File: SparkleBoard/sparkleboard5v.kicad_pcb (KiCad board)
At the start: 2 copper layers, 33.4 x 29.7 mm, 33 parts, among them J3 Conn_01x04_Pin, J4 Conn_01x02_Pin, J5 Conn_01x02_Pin, U1 C9900066641, U2 AONR21307, U3 HUSB238, U6 AP63205WU

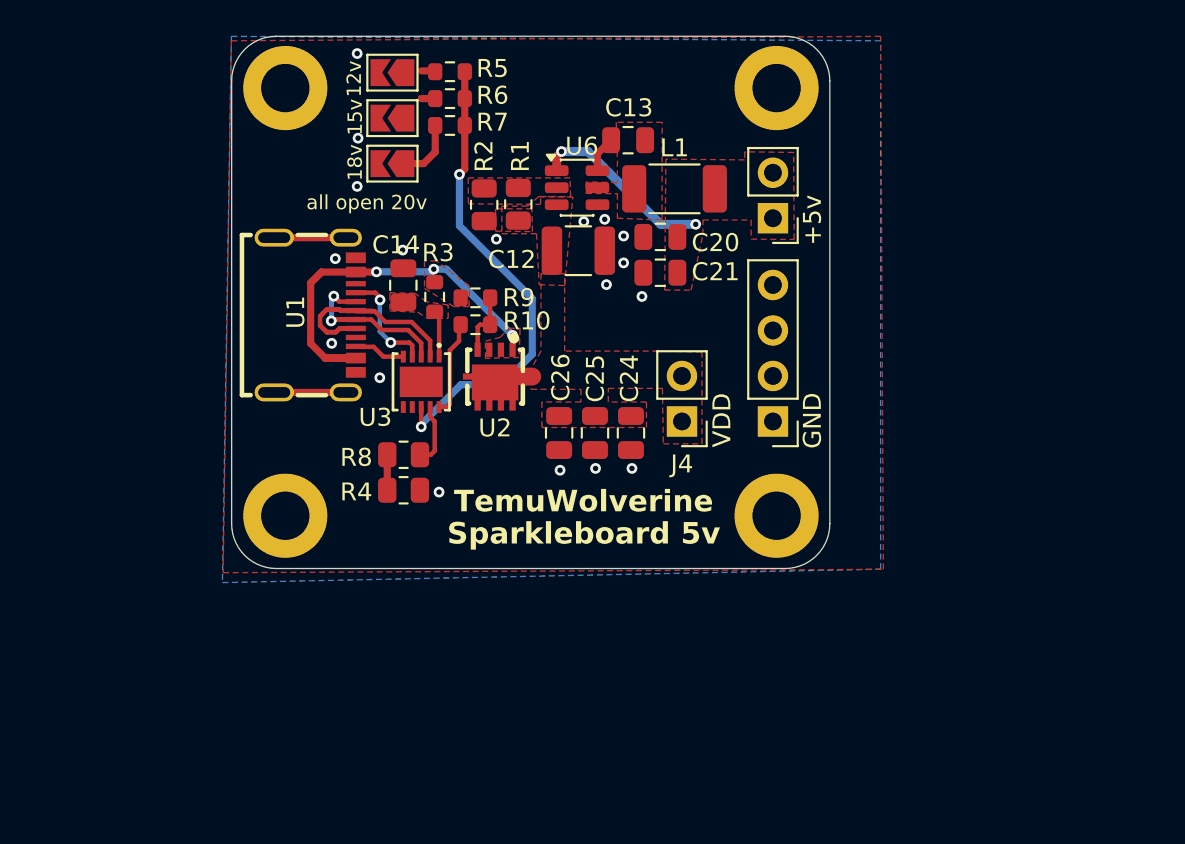
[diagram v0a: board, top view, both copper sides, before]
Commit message: redesigned board around HUSB238*A*. Pin compatible, but non-A revision seems to be EOL. HUSB238A has different footprint (QFN?) Enlarged board to make more logical groupings of components (ie ISET/VSET) USB connector (C9900066641) is also EOL and should be replaced before MFG
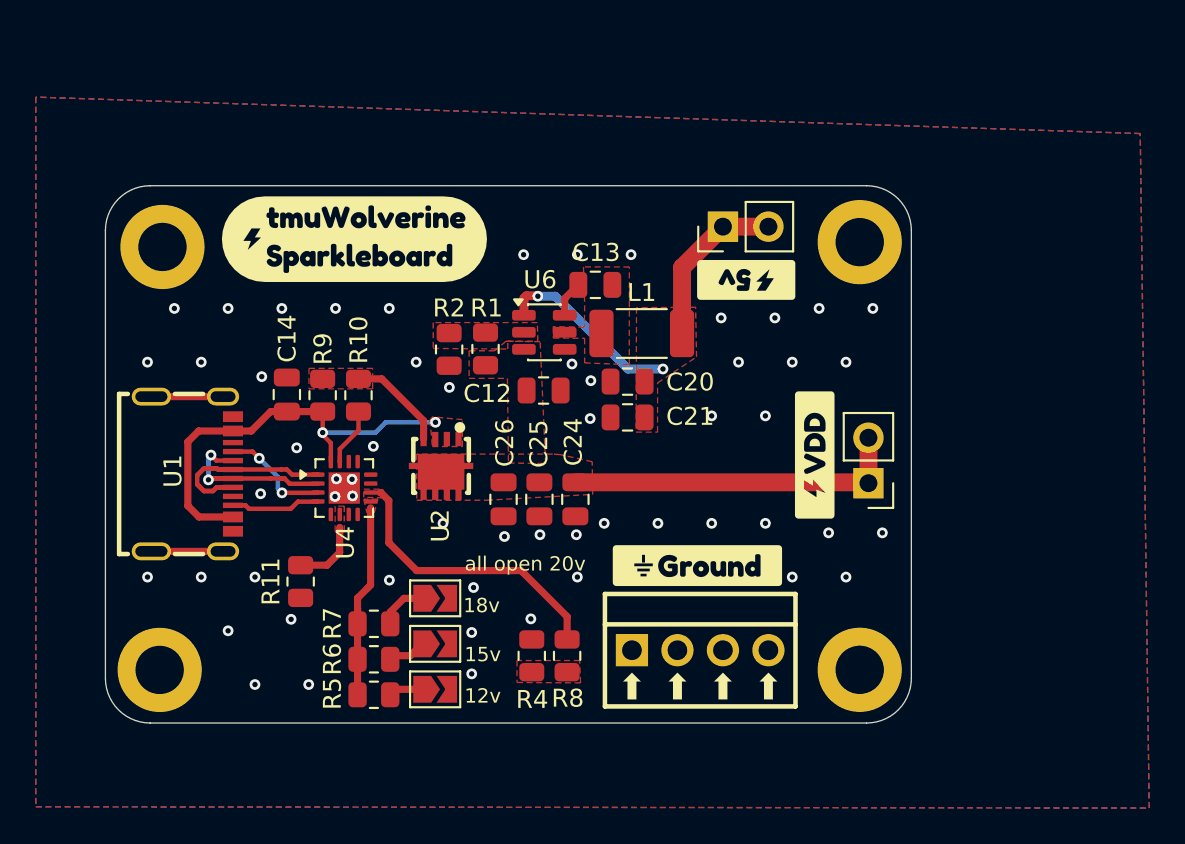
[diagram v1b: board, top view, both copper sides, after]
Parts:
- removed R3: 10, Resistor_SMD:R_0603_1608Metric
- removed U3: HUSB238, EasyEDA_Lib:TDFN-10_L3.0-W3.0-P0.50-TL-EP
- added R11: 900k, Resistor_SMD:R_0805_2012Metric, F.Cu at (96.1, 76.9)
- added U4: HUSB238A-xxxxx-QN16R, Package_DFN_QFN:WQFN-16-1EP_3x3mm_P0.5mm_EP1.75x1.75mm, F.Cu at (98.5, 71.7)
- added kobee-studio-6A969DA9: Kobee Studio, kobee-studio-6A969D7E, F.Cu at (99.1, 57.8)
- added kobee-studio-6A9D10D7: Kobee Studio, kobee-studio-6A9D10A2, F.Cu at (120.9, 60.1)
- added kobee-studio-6A9D10E5: Kobee Studio, kobee-studio-6A9D10A2, F.Cu at (118.2, 76.0)
- added kobee-studio-6A9D10F2: Kobee Studio, kobee-studio-6A9D10A2, F.Cu at (124.8, 69.9)
- C12: footprint Capacitor_SMD:C_1210_3225Metric -> Capacitor_SMD:C_0805_2012Metric
- J3: footprint Connector_PinHeader_2.54mm:PinHeader_1x04_P2.54mm_Vertical -> EasyEDA_Lib:CONN-TH_DB125-2.54-4P-GN
- R10, R5, R6, R7, R9: footprint Resistor_SMD:R_0603_1608Metric -> Resistor_SMD:R_0805_2012Metric
- moved R5 35.0 mm to (100.1, 83.3), turned to 0 degrees
- moved JP2 34.5 mm to (103.6, 82.9), turned to 0 degrees
- moved R6 31.6 mm to (100.1, 81.3), turned to 0 degrees
- moved JP3 29.4 mm to (103.6, 80.4), turned to 0 degrees
- moved R7 28.1 mm to (100.1, 79.3), turned to 0 degrees
- moved JP4 24.4 mm to (103.6, 77.9), turned to 0 degrees
- moved R8 14.5 mm to (110.9, 81.1), turned to -90 degrees
- moved J3 13.4 mm to (118.4, 80.8)
- moved R4 11.7 mm to (109.0, 81.1), turned to -90 degrees
- moved H1 11.2 mm to (88.3, 58.2)
- moved U1 11.2 mm to (90.0, 70.9)
- moved H3 11.1 mm to (88.2, 81.9)
- moved J4 11.0 mm to (127.8, 71.4)
- moved R9 10.1 mm to (97.3, 66.5), turned to -90 degrees
- moved H2 9.78 mm to (127.3, 58.0)
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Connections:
- C14 pad 2: Net-(U3-VIN) -> /VBUS
- U1 pad EH1: unconnected-(U1-PadEH1) -> GND
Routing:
- net VDD: track 0.89 -> 19.7 mm
- net VSET: track 26.6 -> 11.6 mm, vias 2 -> 0
- net ISET: track 3.47 -> 16.0 mm
- net +5V: track 11.5 -> 19.9 mm
- net unconnected-(U1-PadEH1): track 8.00 -> 0.00 mm
- net GND: track 0.00 -> 8.00 mm, vias 18 -> 57
- net Net-(U4-~{DEBUG}): track 0.00 -> 3.88 mm
- net Net-(U3-VIN): track 2.61 -> 0.00 mm
- net CC2: track 2.89 -> 5.02 mm
- net Net-(U2-G): track 3.52 -> 5.63 mm
- net Net-(U4-GATE): track 5.32 -> 3.24 mm
- net /VBUS: track 22.1 -> 24.1 mm, vias 3 -> 2
- net Net-(R4-Pad2): track 1.98 -> 0.00 mm
- net USBC_D+: track 15.9 -> 14.2 mm
- net Net-(JP3-A): track 0.79 -> 2.14 mm
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- added copper zone on F.Cu, net ISET
- added copper zone on F.Cu, net Net-(R4-Pad2)
- added copper zone on F.Cu, net Net-(U2-G)
- added copper zone on F.Cu, net Net-(U4-~{DEBUG})
- added copper zone on F.Cu, net VSET
- removed copper zone on F.Cu, net Net-(U3-VIN)
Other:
- board size 33.4 x 29.7 mm -> 45 x 30 mm
- board text removed: "+5v"
- board text removed: "GND"
- board text removed: "Sparkleboard 5v"
- board text removed: "TemuWolverine"
- board text removed: "VDD"
